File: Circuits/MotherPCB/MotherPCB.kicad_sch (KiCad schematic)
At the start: 3 parts, among them U18 ESP32-DEVKITC-32E, U20 Teensy_4.1

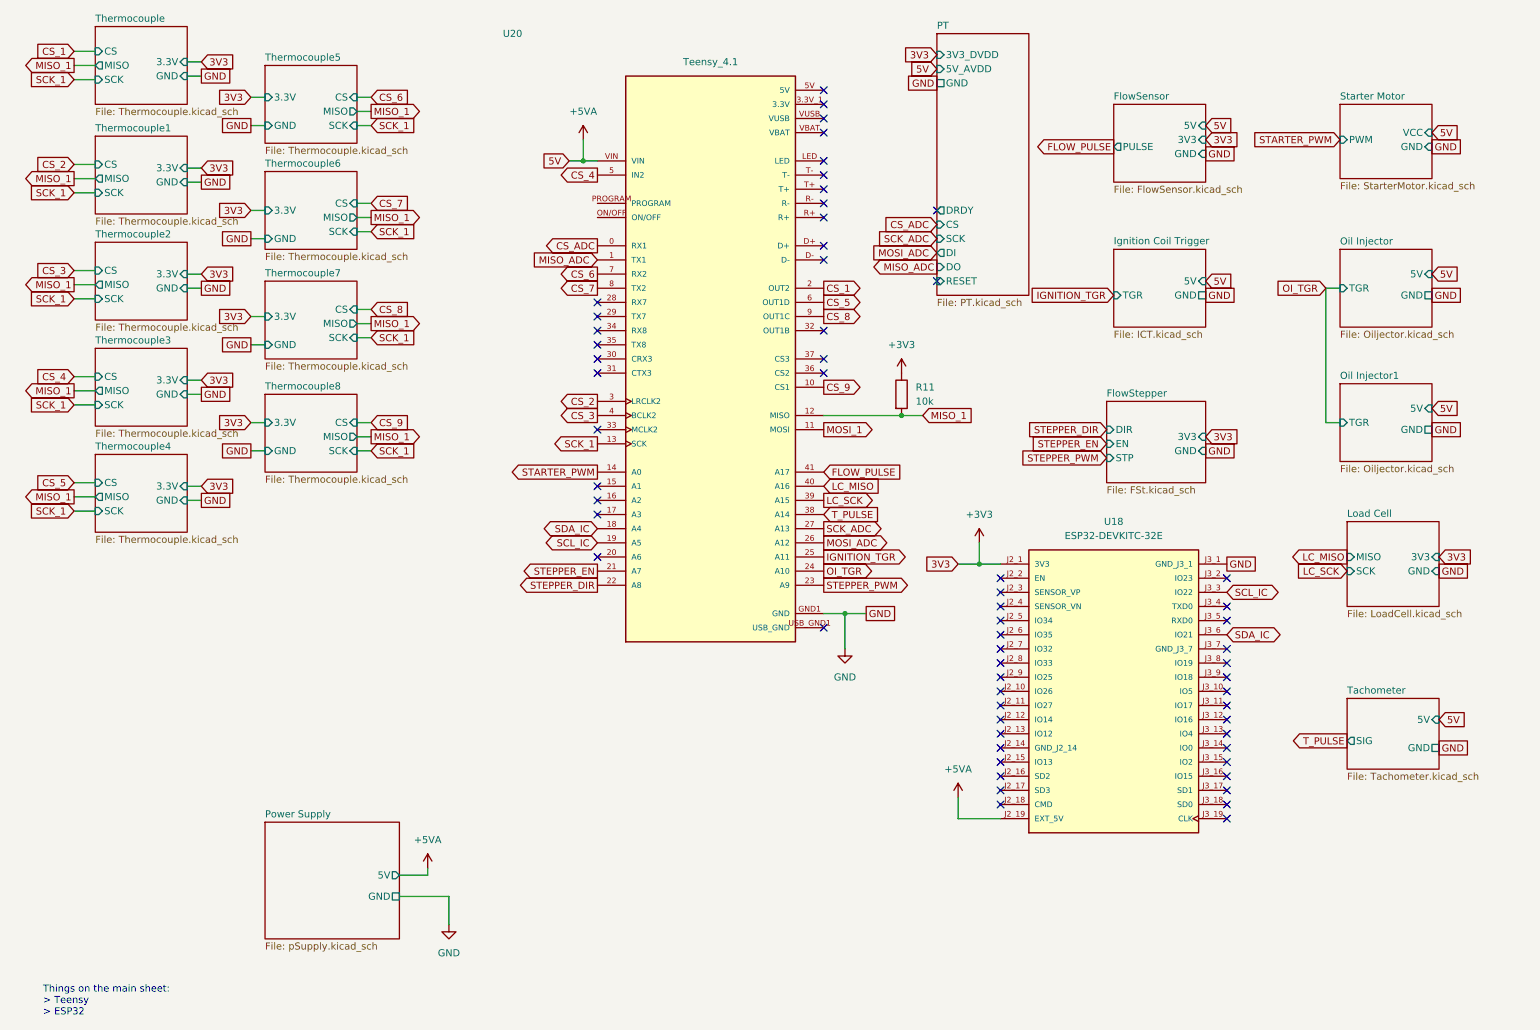
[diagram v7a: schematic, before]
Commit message: This commit comprises of multiple changes 1. Final MotherPCB (Redesigned by Akshay, only pushed to GitHub by me) 2. PCB for interfacing with the Ethernet MagJack 3. Code for Pressure Transducer data acquisition 4. Inclusion of an ADS1263 Library modified to allow use of SPI1 5. Code for Tachometer re-written as class with static member functions
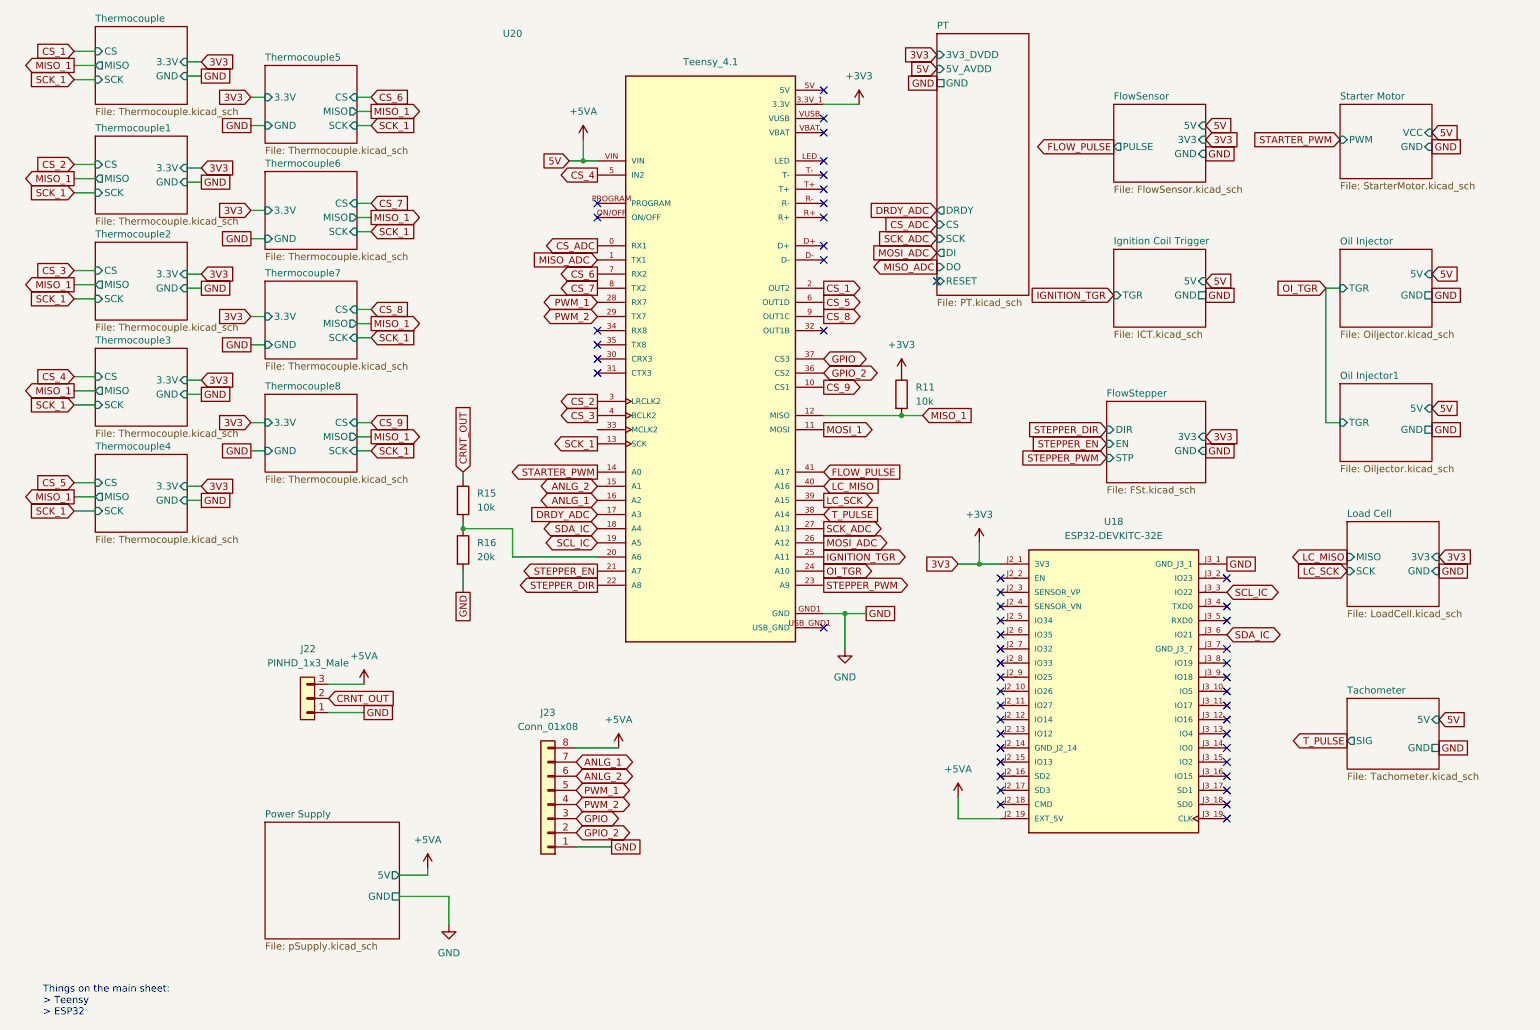
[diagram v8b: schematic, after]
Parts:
- added J22: PINHD_1x3_Male, Connector_PinHeader_2.54mm:PinHeader_1x03_P2.54mm_Vertical, symbol PCM_SL_Pin_Headers:PINHD_1x3_Male
- added J23: Conn_01x08, Connector_PinHeader_2.54mm:PinHeader_1x08_P2.54mm_Vertical, symbol Connector_Generic:Conn_01x08
- added R15: 10k, Resistor_THT:R_Axial_DIN0207_L6.3mm_D2.5mm_P7.62mm_Horizontal, symbol Device:R
- added R16: 20k, Resistor_THT:R_Axial_DIN0207_L6.3mm_D2.5mm_P7.62mm_Horizontal, symbol Device:R
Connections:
- net 3.3V is gone; now on net +3V3: U20.3.3V_1 (3.3V), U20.3.3V_2 (3.3V), U20.3.3V_3 (3.3V)
- net +5VA: now also J22.3, J23.8 (Pin_8)
- net GND: now also J22.1, J23.1 (Pin_1), R16.2
- net ANLG_2: now reaches U20.15 (A1)
- net ANLG_2: now also J23.6 (Pin_6)
- net ANLG_1: now reaches U20.16 (A2)
- net ANLG_1: now also J23.7 (Pin_7)
- net DRDY_ADC: now reaches U20.17 (A3)
- net at U20.20 (A6): now also R15.2, R16.1
- net PWM_1: now reaches U20.28 (RX7)
- net PWM_1: now also J23.5 (Pin_5)
- net PWM_2: now reaches U20.29 (TX7)
- net PWM_2: now also J23.4 (Pin_4)
- net GPIO_2: now reaches U20.36 (CS2)
- net GPIO_2: now also J23.2 (Pin_2)
- net GPIO: now reaches U20.37 (CS3)
- net GPIO: now also J23.3 (Pin_3)
- new net CRNT_OUT: J22.2, R15.1
- no-connect marks 61 -> 52
